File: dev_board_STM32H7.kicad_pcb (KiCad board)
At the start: 2 copper layers, 40.9 x 68.6 mm, 50 parts, among them J1 USB_C_Receptacle_USB2.0_16P, J2 Left, J3 Right, J4 Conn_01x05_Pin, J5 Conn_01x04, J6 Conn_01x08, SW1 SW_DIP_x01, SW2 SW_DIP_x01, SW3 SW_DIP_x01, U1 AMS1117-3.3, U2 STM32H750VBTx, U3 W25Q32JVSS, Y1 25M@20pF, Y2 32.768k@10pF

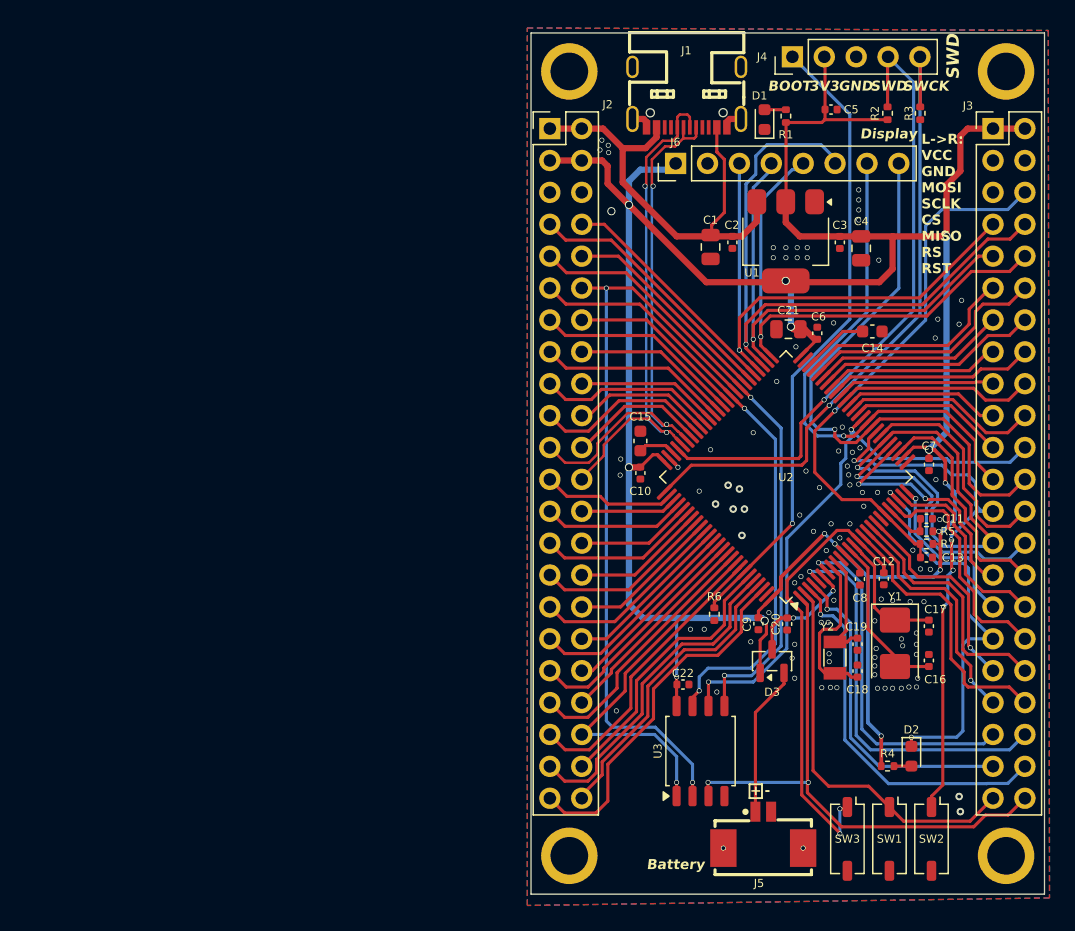
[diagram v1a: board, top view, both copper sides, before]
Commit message: Modify line width of power strack
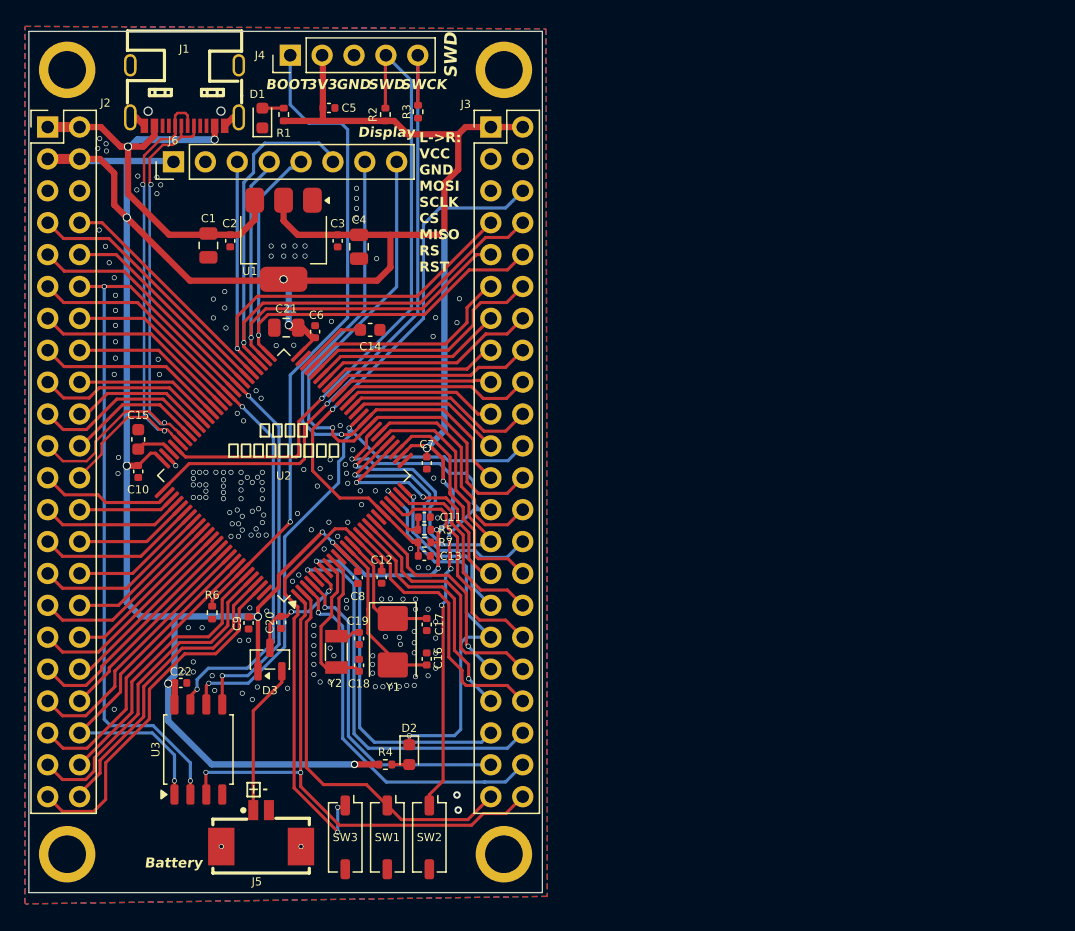
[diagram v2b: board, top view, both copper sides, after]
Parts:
- moved C9 40.6 mm to (78.6, 107.1)
- moved C20 40.3 mm to (81.2, 107.0)
- moved C7 40.0 mm to (92.8, 94.3)
- moved C1 40.0 mm to (75.4, 77.0)
- moved C10 40.0 mm to (69.8, 95.0)
- moved C11 40.0 mm to (92.6, 98.7)
- moved C13 40.0 mm to (92.6, 101.7)
- moved C14 40.0 mm to (88.3, 83.7)
- moved C15 40.0 mm to (69.8, 92.5)
- moved C16 40.0 mm to (92.8, 109.9)
- moved C17 40.0 mm to (92.8, 107.2)
- moved C2 40.0 mm to (77.1, 76.6)
- moved C21 40.0 mm to (81.6, 83.5)
- moved C22 40.0 mm to (73.2, 111.8)
- moved C3 40.0 mm to (85.7, 76.6)
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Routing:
- net +3V3: track 228.2 -> 240.1 mm
- net /MCU_STM32H7/MCU_BOOT0: track 50.3 -> 51.8 mm
- net +5V: track 36.8 -> 35.7 mm, vias 0 -> 2
- net Net-(U2-PC14): track 12.9 -> 11.8 mm
- net /MCU_STM32H7/PSPI.RS: track 44.3 -> 44.8 mm
- net GND: track 4.43 -> 3.91 mm, vias 104 -> 183
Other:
- board text added: "0"
- board text added: "0 mm"
- board text added: "0.01 mm"
- board text added: "0.02"
- board text added: "0.035 mm"
- board text added: "0.1000 mm / 0.1000 mm"
- board text added: "0.3000 mm"
- board text added: "1"
- board text added: "1.51 mm"
- board text added: "1.6000 mm"
- board text added: "2"
- board text added: "3.3"
- board text added: "4.5"
- board text added: "40.9000 mm x 68.6000 mm"
- board text added: "B.Cu"
- board text added: "B.Mask"
- board text added: "B.Paste"
- board text added: "B.Silkscreen"
- board text added: "BOARD CHARACTERISTICS"
- board text added: "Board Thickness:"
- board text added: "Board overall dimensions:"
- board text added: "Bottom Silk Screen"
- board text added: "Bottom Solder Mask"
- board text added: "Bottom Solder Paste"
- board text added: "Castellated pads:"
- board text added: "Color"
- board text added: "Copper Finish:"
- board text added: "Copper Layer Count:"
- board text added: "Edge card connectors:"
- board text added: "Epsilon R"
- board text added: "F.Cu"
- board text added: "F.Mask"
- board text added: "F.Paste"
- board text added: "F.Silkscreen"
- board text added: "FR4"
- board text added: "FR4 natural"
- board text added: "Impedance Control:"
- board text added: "Layer Name"
- board text added: "Loss Tangent"
- board text added: "Material"
- board text added: "Min hole diameter:"
- board text added: "Min track/spacing:"
- board text added: "No"
- board text added: "None"
- board text added: "Not specified"
- board text added: "Plated Board Edge:"
- board text added: "Thickness (mm)"
- board text added: "Top Silk Screen"
- board text added: "Top Solder Mask"
- board text added: "Top Solder Paste"
- board text added: "Type"
- board text added: "copper"
- board text added: "core"
- board text added: "介质 1"
- board text added: "拆芯片？ 拆了就不给退了喔！"
